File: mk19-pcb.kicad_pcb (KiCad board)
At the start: 2 copper layers, 130 x 85 mm, 96 parts, among them J10 Conn_01x02_Socket, J11 Conn_01x02_Socket, J12 Conn_01x02_Socket, J4 Conn_01x02_Socket, J5 Conn_01x02_Socket, J6 Conn_01x02_Socket, J7 Conn_01x02_Socket, J9 Conn_01x02_Socket, T1 Conn_01x01_Socket, T10 Conn_01x01_Socket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

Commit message: feb16 work, almost ready to start running traces
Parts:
- removed COL_JOIN3: Conn_01x02_Socket, Connector_PinSocket_2.54mm:PinSocket_1x02_P2.54mm_Vertical
- removed G2, G3, G6, T1, T2, T3, T4, T7, T8: Conn_01x01_Socket, Connector_Pin:Pin_D1.0mm_L10.0mm
- removed J5, J6: Conn_01x02_Socket, Connector_JST:JST_EH_B2B-EH-A_1x02_P2.50mm_Vertical
- added GPIO1: Conn_01x03_Socket, Connector_PinSocket_2.54mm:PinSocket_1x03_P2.54mm_Vertical, F.Cu at (128.2, 71.3)
- added J1: Conn_01x02_Socket, Connector_JST:JST_EH_B2B-EH-A_1x02_P2.50mm_Vertical, F.Cu at (181.8, 96.2)
- added J2: Conn_01x02_Socket, Connector_JST:JST_EH_B2B-EH-A_1x02_P2.50mm_Vertical, F.Cu at (176.7, 96.2)
- added MISO_PULL1: Conn_01x02_Socket, Connector_PinSocket_2.54mm:PinSocket_1x02_P2.54mm_Vertical, F.Cu at (127.9, 93.5)
- added PWR-EXT-IN1: Conn_01x02_Socket, Connector_JST:JST_EH_B2B-EH-A_1x02_P2.50mm_Vertical, F.Cu at (164.7, 92.5)
- added PWR-OUT6: Conn_01x03_Socket, Connector_PinSocket_2.54mm:PinSocket_1x03_P2.54mm_Vertical, F.Cu at (164.4, 85.1)
- moved AUDIO1 107.8 mm to (97.5, 54.3), turned to 180 degrees
- moved PWR-OUT2 89.6 mm to (180.1, 79.1)
- moved SCREEN1 83.6 mm to (193.7, 56.0)
- moved PWR-OUT1 82.9 mm to (175.4, 80.2)
- moved J7 81.8 mm to (171.6, 96.2)
- moved C9 78.9 mm to (178.1, 89.2)
- moved C7 78.3 mm to (172.0, 89.4)
- moved C8 77.8 mm to (183.6, 89.3)
- moved RESET1 75.1 mm to (96.1, 60.7)
- moved ADC1 54.8 mm to (162.6, 78.2), turned to 90 degrees
- moved R6 52.1 mm to (115.0, 126.9), turned to 0 degrees
- moved DBG1 51.2 mm to (147.6, 107.9), turned to 180 degrees
- moved R7 49.5 mm to (115.1, 129.3), turned to 0 degrees
- moved CYBOARD-MACRO1 49.0 mm to (139.6, 124.7)
- moved CYBOARD-MAIN1 48.7 mm to (151.4, 125.0)
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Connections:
- C7 pad 1: VCC -> LED_5V
- C8 pad 1: VCC -> LED_5V
- C9 pad 1: VCC -> LED_5V
- J7 pad 2: VCC -> LED_5V
- PICO1 pad 34: LED_3v3_DI -> LED_DI_3v3
- T9 pad 1: LED_DI_3.3V -> LED_DI_3v3

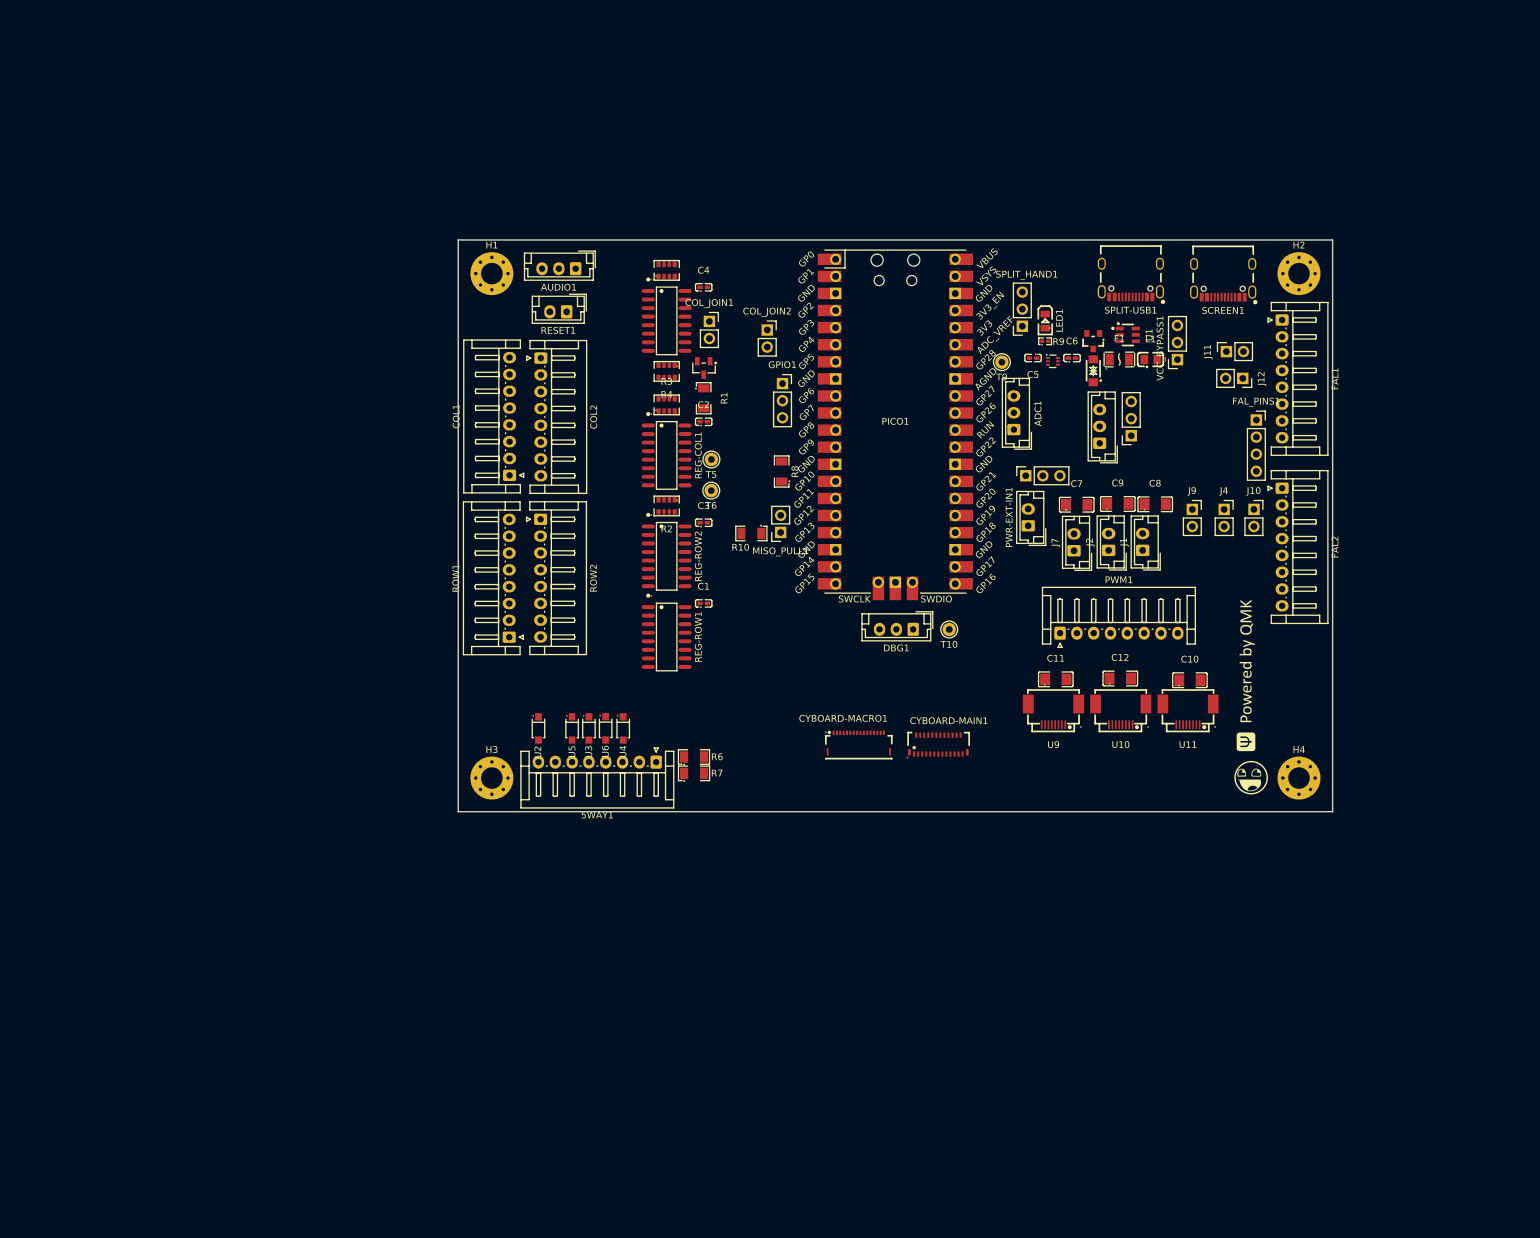
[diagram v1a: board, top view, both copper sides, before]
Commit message: first draft done - needs work on led signal flow, silkscreen, falcon row-col thing.
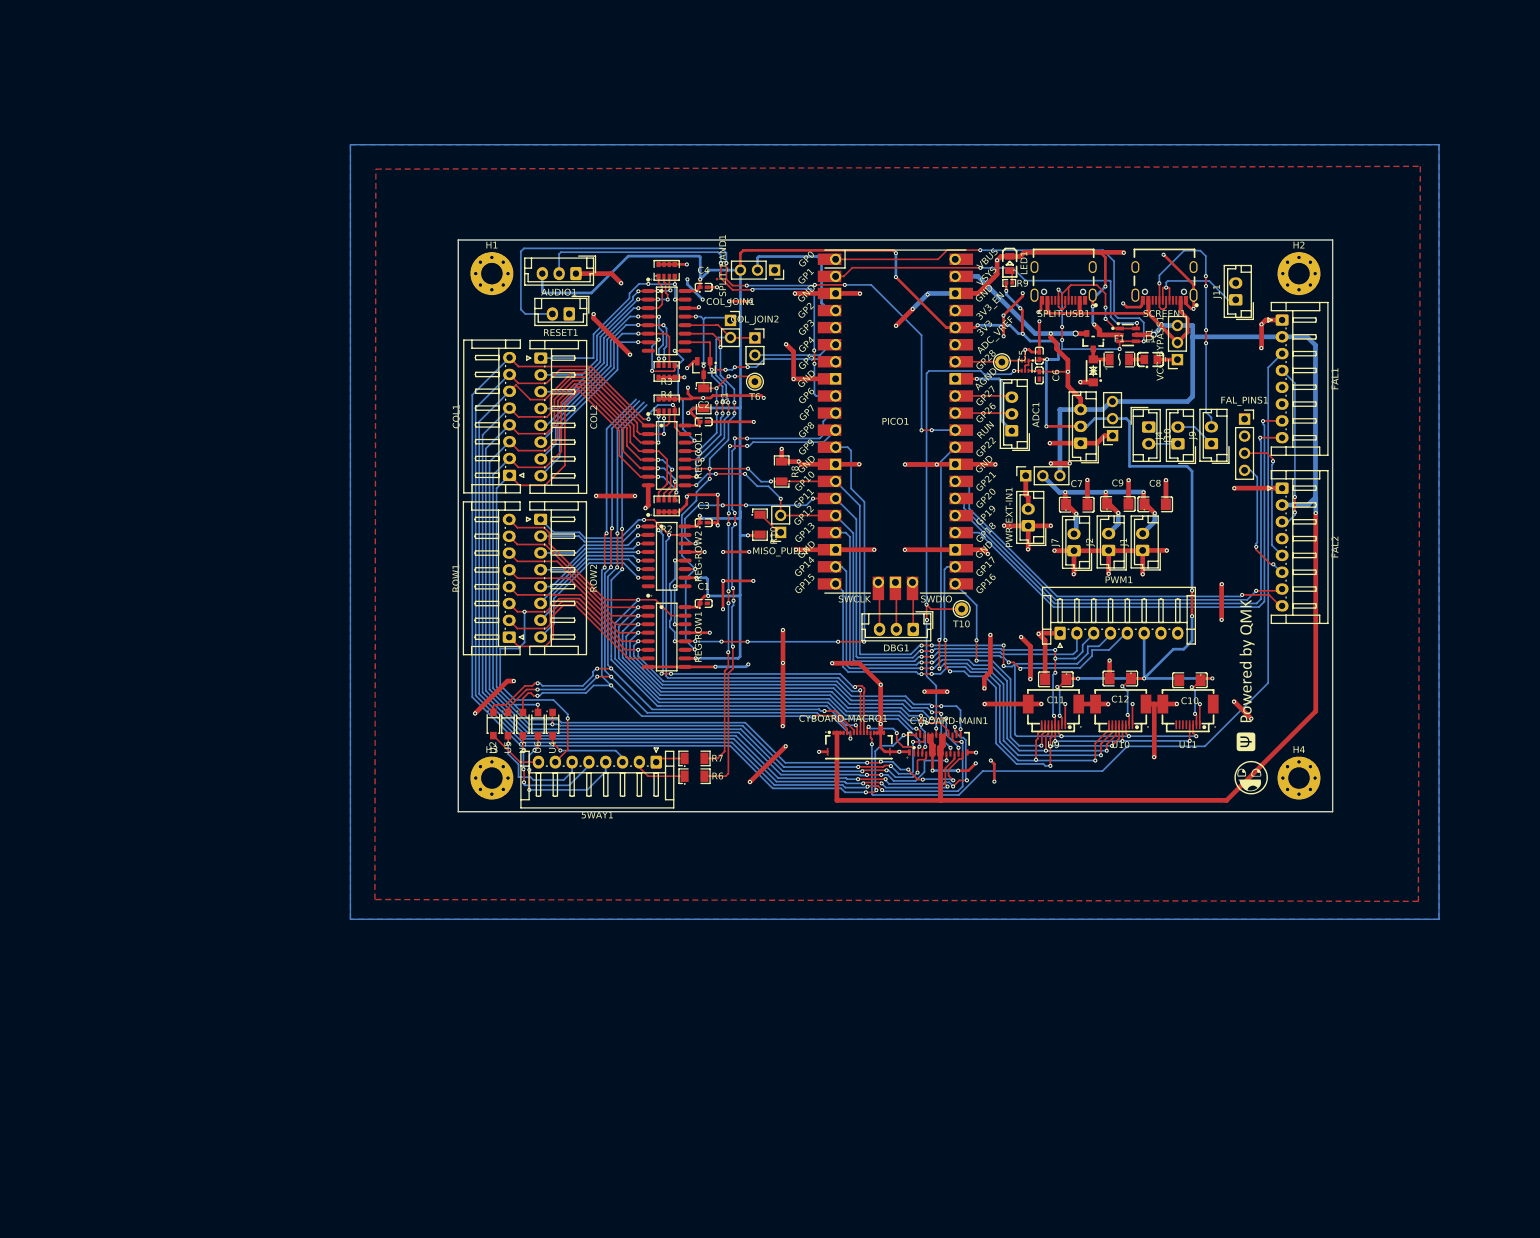
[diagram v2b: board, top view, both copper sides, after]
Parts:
- removed GPIO1: Conn_01x03_Socket, Connector_PinSocket_2.54mm:PinSocket_1x03_P2.54mm_Vertical
- removed J12: Conn_01x02_Socket, Connector_PinSocket_2.54mm:PinSocket_1x02_P2.54mm_Vertical
- removed T5: Conn_01x01_Socket, Connector_Pin:Pin_D1.0mm_L10.0mm
- J10, J11, J4, J9: footprint Connector_PinSocket_2.54mm:PinSocket_1x02_P2.54mm_Vertical -> Connector_JST:JST_EH_B2B-EH-A_1x02_P2.50mm_Vertical
- moved SPLIT_HAND1 37.8 mm to (127.0, 54.5), turned to -90 degrees
- moved J10 19.9 mm to (182.7, 77.8), turned to -90 degrees
- moved T6 17.4 mm to (124.1, 71.1)
- moved J4 11.9 mm to (187.0, 80.3), turned to 90 degrees
- moved U4 10.5 mm to (94.0, 122.0)
- moved R9 10.2 mm to (161.9, 56.4)
- moved J9 10.2 mm to (192.0, 80.3), turned to 90 degrees
- moved U6 10.1 mm to (91.9, 122.0)
- moved LED1 10.1 mm to (162.0, 53.5)
- moved SPLIT-USB1 10.0 mm to (170.0, 56.5)
- moved U3 9.84 mm to (89.6, 122.0)
- moved U5 9.56 mm to (87.4, 122.0)
- moved SCREEN1 8.74 mm to (185.0, 56.5)
- moved J11 7.82 mm to (195.6, 58.9)
- moved U2 6.73 mm to (85.2, 122.0)
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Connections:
- COL1 pad 1: col0 -> col7
- COL1 pad 2: col1 -> col6
- COL1 pad 3: col2 -> col5
- COL1 pad 4: col3 -> col4
- COL1 pad 5: col4 -> col3
- COL1 pad 6: col5 -> col2
- COL1 pad 7: col6 -> col1
- COL1 pad 8: col7 -> col0
- J11 pad 1: LED_SCREEN_DI -> LED_SCREEN_DO
- J11 pad 2: LED_EXTRA_DI -> unconnected-(J11-Pin_2-Pad2)
- LED-LVL1 pad 3: LED_3v3_DI -> LED_DI_3v3
- PICO1 pad 10: GPIO7 -> rkjxt-a
- PICO1 pad 11: GPIO8 -> rkjxt-b
- ROW1 pad 1: row0 -> row7
- ROW1 pad 2: row1 -> row6
- ROW1 pad 3: row2 -> row5
- ROW1 pad 4: row3 -> row4
- ROW1 pad 5: row4 -> row3
- ROW1 pad 6: row5 -> row2
- ROW1 pad 7: row6 -> row1
- ROW1 pad 8: row7 -> row0
- SCREEN1 pad A7: LED_EXT_DI -> LED_SCREEN_DO
- SCREEN1 pad B7: LED_EXT_DI -> LED_SCREEN_DO
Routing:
- net GND: track 0.00 -> 515.7 mm, vias 0 -> 118
- net +3V3: track 0.00 -> 358.6 mm, vias 0 -> 26
- net VCC: track 0.00 -> 276.3 mm, vias 0 -> 5
- net SPI1_CLK: track 0.00 -> 198.0 mm, vias 0 -> 16
- net col3: track 0.00 -> 168.8 mm, vias 0 -> 7
- net col1: track 0.00 -> 168.0 mm, vias 0 -> 3
- net col0: track 0.00 -> 166.6 mm, vias 0 -> 5
- net col7: track 0.00 -> 162.6 mm, vias 0 -> 8
- net col2: track 0.00 -> 161.8 mm, vias 0 -> 5
- net col4: track 0.00 -> 160.6 mm, vias 0 -> 3
- net col6: track 0.00 -> 157.3 mm, vias 0 -> 6
- net col5: track 0.00 -> 155.3 mm, vias 0 -> 5
- net col10: track 0.00 -> 134.1 mm, vias 0 -> 9
- net col8: track 0.00 -> 132.1 mm, vias 0 -> 8
- net SPI1_MOSI: track 0.00 -> 131.6 mm, vias 0 -> 13
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- added copper zone on B.Cu, net GND
- added copper zone on F.Cu, net GND

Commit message: ready for review
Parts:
- removed FAL_PINS1: Conn_01x04_Socket, Connector_PinSocket_2.54mm:PinSocket_1x04_P2.54mm_Vertical
- removed T6, T9: Conn_01x01_Socket, Connector_Pin:Pin_D1.0mm_L10.0mm
- added LOGO5: **REF, ct-kicad:mk19-qr-logo-12mm, B.Cu at (116.9, 127.7)
- moved LOGO1 96.2 mm to (102.4, 118.3)
- moved LOGO3 96.1 mm to (102.3, 118.3)
- moved LOGO2 80.8 mm to (116.5, 120.0), turned to 0 degrees
- moved LOGO4 80.6 mm to (116.7, 120.1), turned to 180 degrees
- moved R10 6.66 mm to (127.9, 98.2)
- moved RESET1 1.85 mm to (95.0, 59.9)
- moved PWR-OUT2 1.35 mm to (178.1, 80.2)
- moved PWR-OUT1 0.98 mm to (173.5, 80.2)
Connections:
- FAL1 pad 5: fal1-row -> row4
- FAL1 pad 6: fal1-col -> col6
- FAL2 pad 4: LED_INDICATORS_DI -> LED_SLATS_BIG_DI
- FAL2 pad 5: fal2-row -> row4
- FAL2 pad 6: fal2-col -> col7
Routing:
- net col6: track 157.3 -> 274.8 mm, vias 6 -> 12
- net row4: track 84.4 -> 193.5 mm, vias 4 -> 10
- net GND: track 515.7 -> 614.5 mm, vias 118 -> 136
- net col7: track 162.6 -> 238.0 mm, vias 8 -> 10
- net LED_SLATS_BIG_DI: track 0.00 -> 39.1 mm, vias 0 -> 2
- net fal2-row: track 19.6 -> 0.00 mm, vias 1 -> 0
- net col8: track 132.1 -> 151.0 mm, vias 8 -> 6
- net fal2-col: track 18.4 -> 0.00 mm, vias 2 -> 0
- net col9: track 131.0 -> 147.1 mm
- net col10: track 134.1 -> 147.1 mm
- net col11: track 112.7 -> 122.7 mm
- net COL_CS_MOS: track 38.6 -> 31.8 mm, vias 8 -> 6
- net reset: track 100.2 -> 97.1 mm
- net Serial_VBUS: track 41.7 -> 39.9 mm
- net row6: track 82.7 -> 81.4 mm
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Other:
- outline, holes or cut-outs redrawn
- board text added: "0 CL 7"
- board text added: "0 COLS 8"
- board text added: "0 RW 7"
- board text added: "3V"
- board text added: "5V"
- board text added: "7 ROWS 15"
- board text added: "8 CL 15"
- board text added: "8 RW 15"
- board text added: "A"
- board text added: "ADC"
- board text added: "ARCBOARD MK19"
- board text added: "AUD"
- board text added: "B"
- board text added: "BAR"
- board text added: "BIG"
- board text added: "BYPASS"
- board text added: "DEBUG"
- board text added: "DPAD/RKJXT"
- board text added: "EXT-LED"
- board text added: "EXT-PWR"
- board text added: "EXT-PWR-IN"
- board text added: "FAL1"
- board text added: "FAL2"
- board text added: "FL"
- board text added: "GD"
- board text added: "IN"
- board text added: "L | R"
- board text added: "LATCH"
- board text added: "LATCH-JOIN"
- board text added: "LCD1"
- board text added: "LCD2"
- board text added: "LED-PWR"
- board text added: "LED-SIG"
- board text added: "MACRO"
- board text added: "MAIN"
- board text added: "MISO-PULL"
- board text added: "PMW"
- board text added: "RST"
- board text added: "SCREEN"
- board text added: "SM"
- board text added: "SPI"
- board text added: "SPLIT"
- board text added: "X"
- board text added: "r"
- board text added: "v"
- board text added: "v2.0"

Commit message: missed cyboard branding, added a test pin for macro led DI
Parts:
- added LOGO6: **REF, ct-kicad:cyboard-logo-10mm, F.Cu at (159.9, 126.2)
- added LOGO6: **REF, ct-kicad:cyboard-logo-10mm, F.Cu at (130.9, 126.1)
- added T1: Conn_01x01_Socket, Connector_Pin:Pin_D1.0mm_L10.0mm, F.Cu at (126.2, 122.9)
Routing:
- net LED_MACRO_DI: track 10.7 -> 29.3 mm, vias 2 -> 3
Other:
- board text added: "KEYS DI"
- board text added: "MAC DI"

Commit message: more minor fixes
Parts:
- moved J11 2.28 mm to (196.6, 56.8)
- moved C10 0.53 mm to (188.5, 115.0)
- moved C11 0.32 mm to (168.8, 115.0)
- moved C12 0.21 mm to (178.5, 115.0)
- renumbered LOGO6 to LOGO7
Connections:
- PICO1 pad 5: GPIO3 -> LCD3_CS
- U11 pad 5: SPARE_1 -> LCD_RST
- U11 pad 6: SPARE_2 -> LCD_DC
- U11 pad 7: SPARE_3 -> LCD3_CS
- U11 pad 8: SPARE_4 -> LCD_BL
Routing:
- net LCD3_CS: track 0.00 -> 114.2 mm, vias 0 -> 5
- net LCD_BL: track 73.7 -> 91.0 mm, vias 4 -> 5
- net LCD_DC: track 74.8 -> 90.5 mm, vias 4 -> 5
- net LCD_RST: track 61.8 -> 77.0 mm, vias 5 -> 6
- net GND: track 614.5 -> 622.0 mm
- net +3V3: track 358.6 -> 359.6 mm
- net SPI1_MOSI: track 131.6 -> 132.3 mm
- net LED_KEYS_DI: vias 4 -> 3
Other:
- board text added: "DPAD RKJXT"
- board text added: "LCD3"
- board text added: "SR.VBUS BYPASS"
- board text added: "a"
- board text added: "b"
- board text removed: "A"
- board text removed: "B"
- board text removed: "BYPASS"
- board text removed: "DPAD/RKJXT"
- board text removed: "SPI"
